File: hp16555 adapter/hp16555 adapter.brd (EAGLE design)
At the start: 55.5 x 26.7 mm, 50 parts

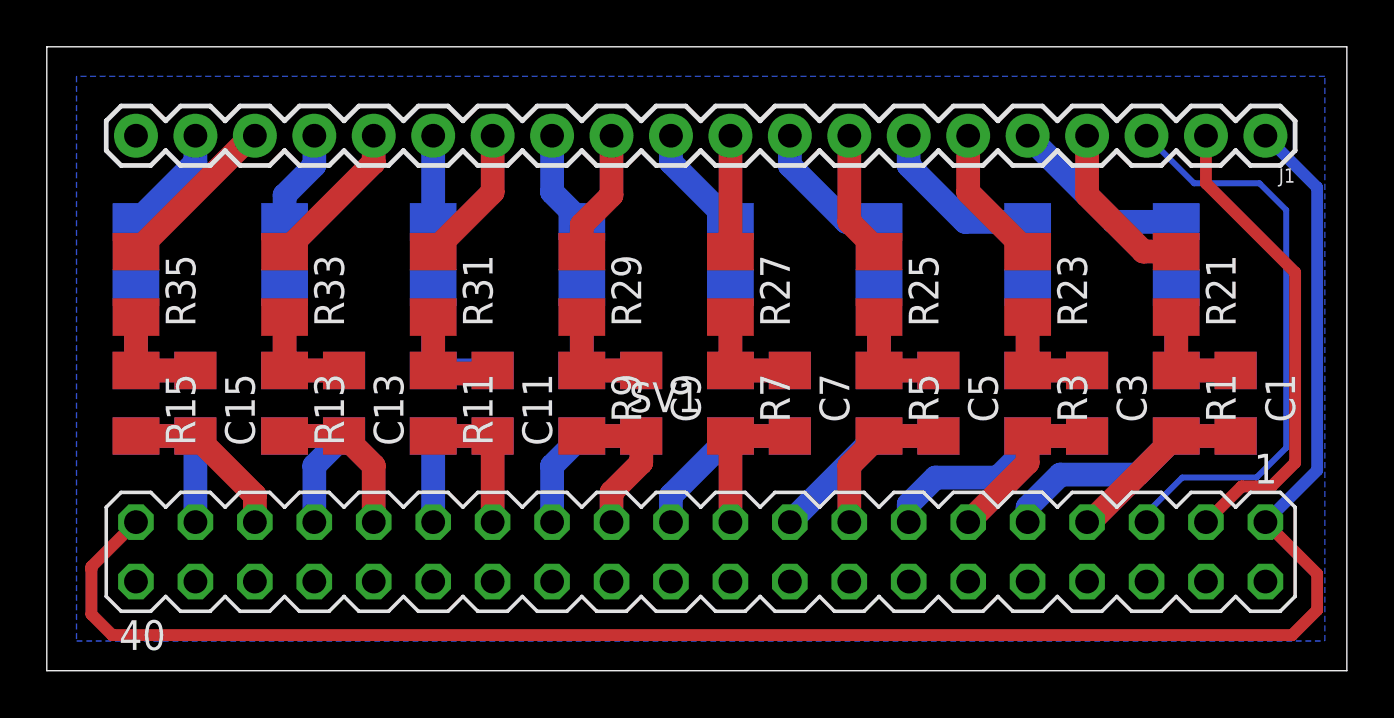
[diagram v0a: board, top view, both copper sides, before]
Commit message: Cleaned up design, made it more compact, entered values into schematic
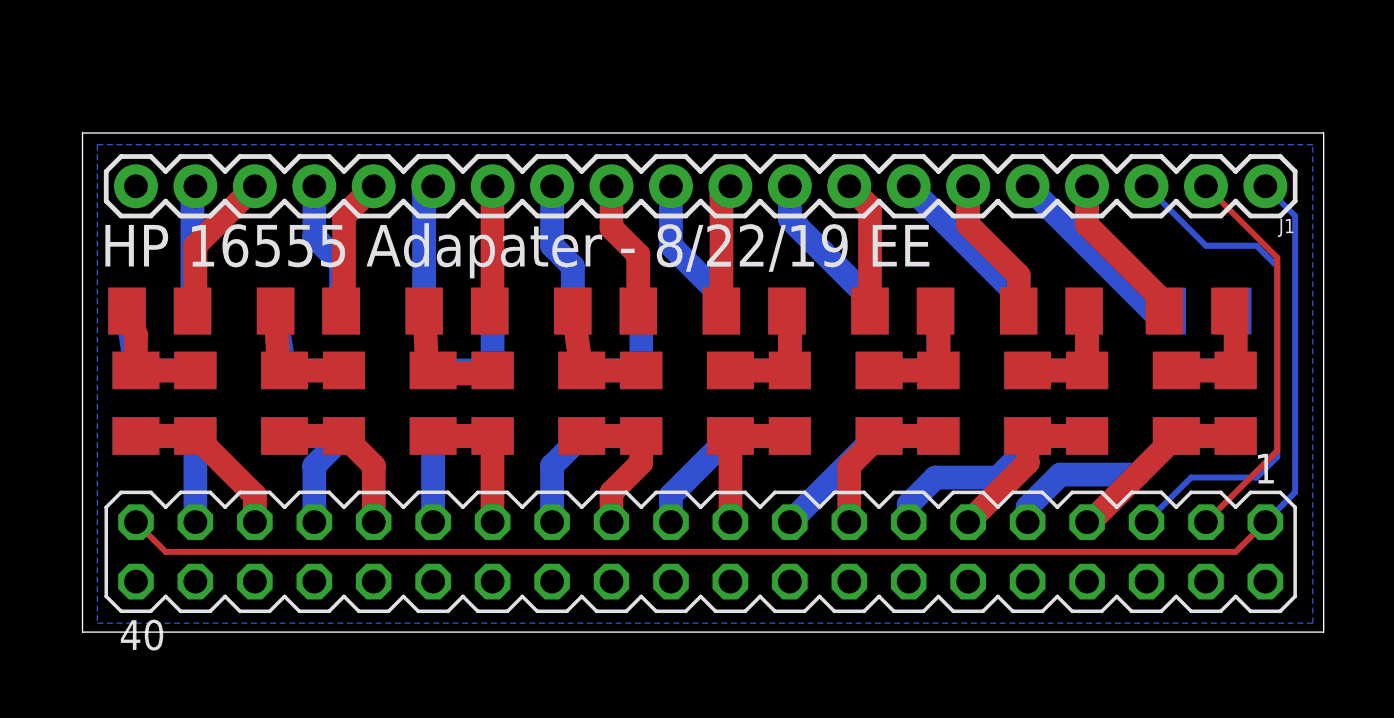
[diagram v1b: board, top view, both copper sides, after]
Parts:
- C1, C10, C11, C12, C13, C14, C15, C16, C2, C3, C4, C5, C6, C7, C8, C9: value (none) -> 8.2pF
- R1, R10, R11, R12, R13, R14, R15, R16, R2, R3, R4, R5, R6, R7, R8, R9: value (none) -> 90K Ohm
- R21, R22, R23, R24, R25, R26, R27, R28, R29, R30, R31, R32, R33, R34, R35, R36: value (none) -> 250 Ohm
- moved R22 2.62 mm to (49.3, 15.4), turned to 180 degrees
- moved R24 2.62 mm to (42.9, 15.4), turned to 180 degrees
- moved R30 2.62 mm to (23.9, 15.4), turned to 180 degrees
- moved R34 2.62 mm to (11.2, 15.4), turned to 0 degrees
- moved R36 2.62 mm to (4.83, 15.4), turned to 0 degrees
- moved R26 2.62 mm to (36.6, 15.4), turned to 180 degrees
- moved R28 2.62 mm to (30.2, 15.4), turned to 180 degrees
- moved R32 2.62 mm to (17.5, 15.4), turned to 180 degrees
- moved J1 2.16 mm to (52.1, 20.7)
- moved R23 1.53 mm to (42.9, 15.4), turned to 0 degrees
- moved R29 1.53 mm to (23.9, 15.4), turned to 180 degrees
- moved R33 1.53 mm to (11.2, 15.4), turned to 180 degrees
- moved R35 1.53 mm to (4.83, 15.4), turned to 180 degrees
- moved R25 1.53 mm to (36.6, 15.4), turned to 0 degrees
- moved R27 1.53 mm to (30.2, 15.4), turned to 0 degrees
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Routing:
- net +5V: track 80.9 -> 64.7 mm
- net CLK1: track 20.4 -> 16.9 mm
- net CLK2: track 25.0 -> 21.9 mm
- net D4-I: track 3.68 -> 5.49 mm
- net D2-I: track 4.21 -> 5.81 mm
- net D8-I: track 4.73 -> 6.23 mm
- net D6-I: track 4.21 -> 5.70 mm
- net N$27: track 6.09 -> 5.11 mm
- net N$25: track 6.09 -> 5.11 mm
- net N$39: track 6.09 -> 5.13 mm
- net N$33: track 6.09 -> 5.13 mm
- net N$31: track 6.09 -> 5.13 mm
- net N$37: track 6.09 -> 5.13 mm
- net N$35: track 6.09 -> 5.13 mm
- net N$29: track 6.09 -> 5.13 mm
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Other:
- board size 55.5 x 26.7 mm -> 53 x 21.3 mm
- board text added: "HP 16555 Adapater - 8/22/19 EE"
